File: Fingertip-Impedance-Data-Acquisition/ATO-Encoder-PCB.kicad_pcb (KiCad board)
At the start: 2 copper layers, 66.2 x 80.8 mm, 29 parts, among them IC1 MCP2561-H_P, J1 DE9_Socket, J2 B2B-XH-A, J3 B2B-XH-A, J4 Conn_01x06, J5 Screw_Terminal_01x02

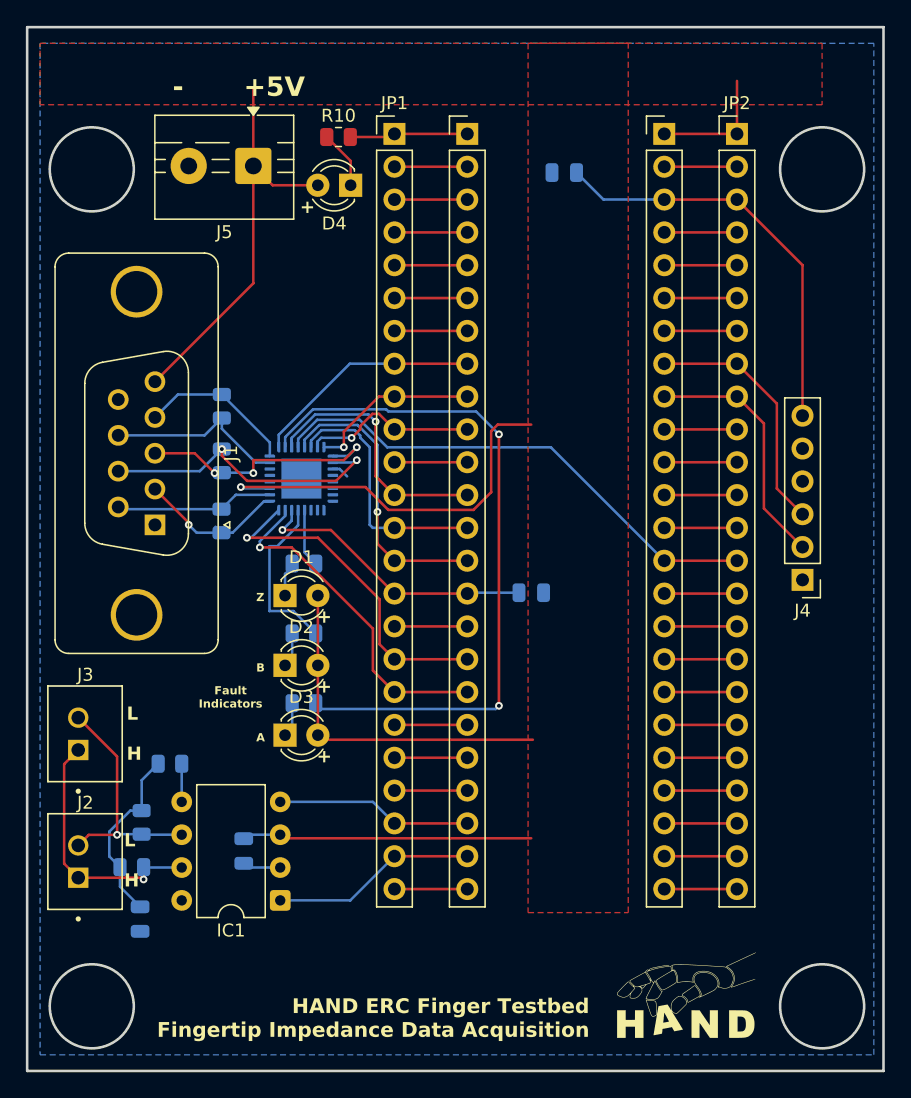
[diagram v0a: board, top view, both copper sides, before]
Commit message: Updated design to be compatible with quadrature decoding without CPU intervention. OSH Park order was updated
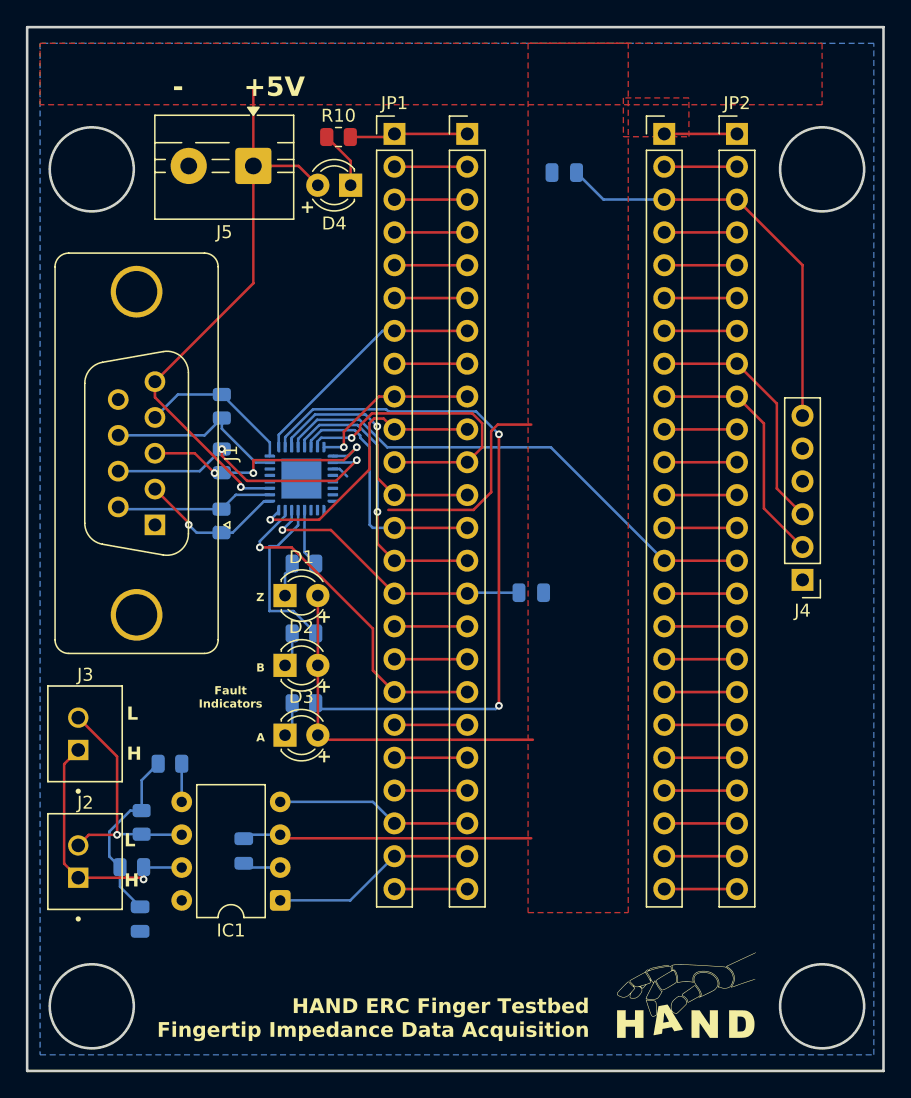
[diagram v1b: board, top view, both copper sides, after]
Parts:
- renumbered C4 to C3, C3 to C4
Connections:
- JP1 pad 10: Encoder Fault -> ZO
- JP1 pad 11: Net-(U$1-P9/PWM/OUT1C) -> Encoder Fault
- JP1 pad 17: ZO -> Net-(U$1-P25/PWM/SDA2/RX6/A11)
- JP1 pad 7: Net-(U$1-P5/PWM/IN2) -> AO
- JP1 pad 8: AO -> Net-(U$1-P6/PWM/OUT1D)
- U$1 pad P10: Net-(U$1-P9/PWM/OUT1C) -> Encoder Fault
- U$1 pad P16: ZO -> Net-(U$1-P25/PWM/SDA2/RX6/A11)
- U$1 pad P6: Net-(U$1-P5/PWM/IN2) -> AO
- U$1 pad P7: AO -> Net-(U$1-P6/PWM/OUT1D)
- U$1 pad P9: Encoder Fault -> ZO
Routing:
- net Encoder Fault: track 13.6 -> 23.7 mm
- net Net-(U$1-P9/PWM/OUT1C): track 5.63 -> 0.00 mm
- net Net-(U$1-P6/PWM/OUT1D): track 0.00 -> 5.63 mm
- net Net-(U$1-P5/PWM/IN2): track 5.63 -> 0.00 mm
- net Net-(U$1-P25/PWM/SDA2/RX6/A11): track 0.00 -> 5.63 mm
- net +5V: track 122.2 -> 116.9 mm
- net ZO: track 26.3 -> 21.9 mm
- net AO: track 17.8 -> 18.9 mm

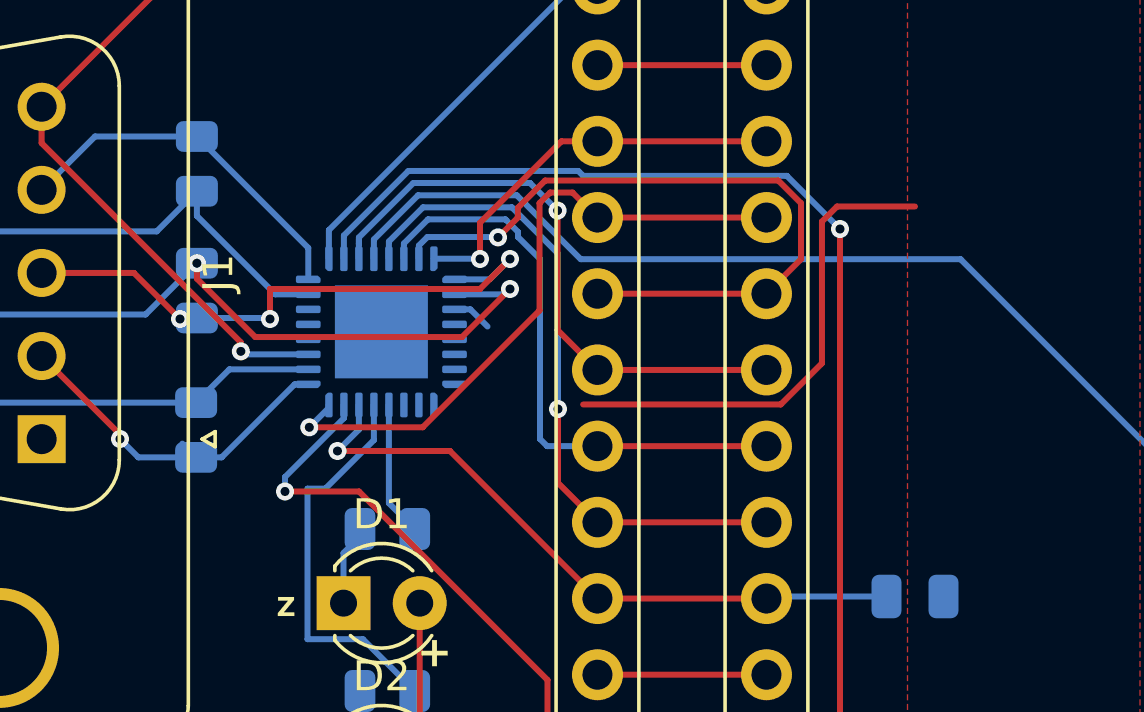
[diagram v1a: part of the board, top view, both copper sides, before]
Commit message: Fixed SPI inteface to MAX chip
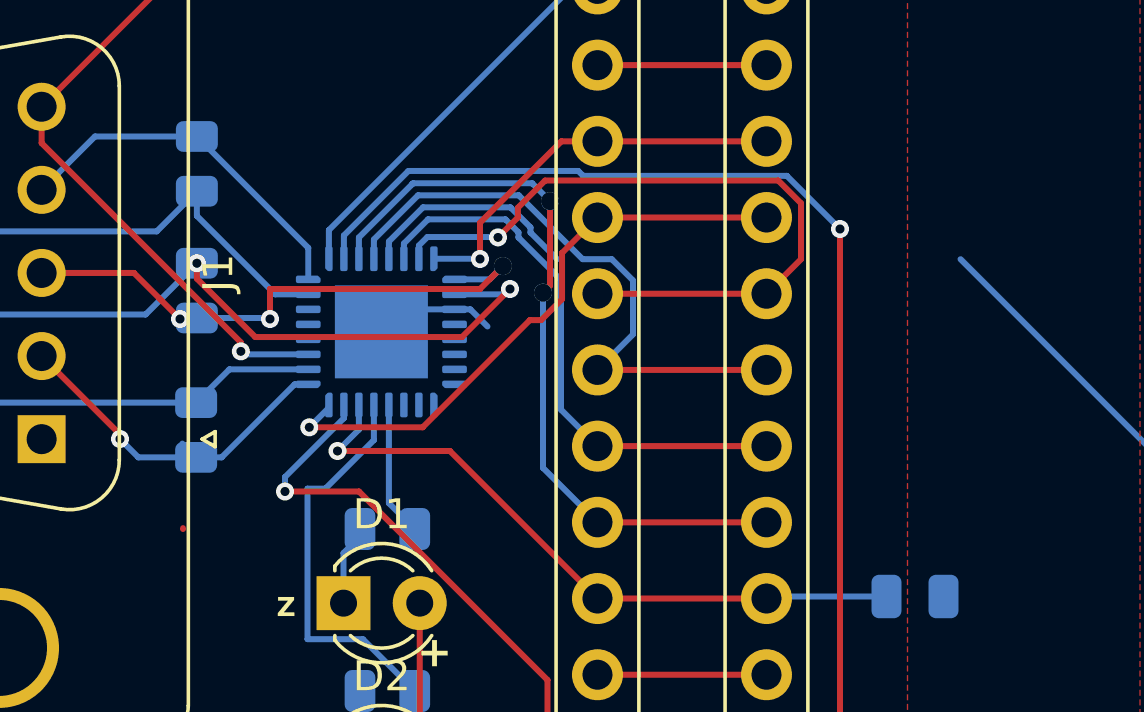
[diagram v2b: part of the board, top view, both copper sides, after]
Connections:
- U1 pad 3: CS -> SDO
- U1 pad 33: (no net) -> GND
- U1 pad 4: CLK -> CS
- U1 pad 5: SDO -> CLK
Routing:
- net +5V: track 116.9 -> 100.3 mm
- net CLK: track 39.7 -> 25.5 mm
- net GND: track 25.2 -> 29.5 mm
- net SDO: track 22.5 -> 25.3 mm, vias 1 -> 2
- net ZO: track 21.9 -> 20.1 mm
- net SDI: track 19.7 -> 18.7 mm
- net Net-(U1-B): track 19.8 -> 19.2 mm
- net CS: track 20.1 -> 20.2 mm, vias 1 -> 0
